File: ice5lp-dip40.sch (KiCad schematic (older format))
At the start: 45 parts, among them J1 Conn_02x04_Odd_Even, J2 Conn_01x20, J3 Conn_01x20, J4 USB_B_Micro, SW1 SW_Push, SW2 SW_Push, U1 AT25D011-SSHF, U2 MIC5355-S4YMME, U3 ICE5LP4K-SG48, X1 ECS-2520MV-500-BN-TR

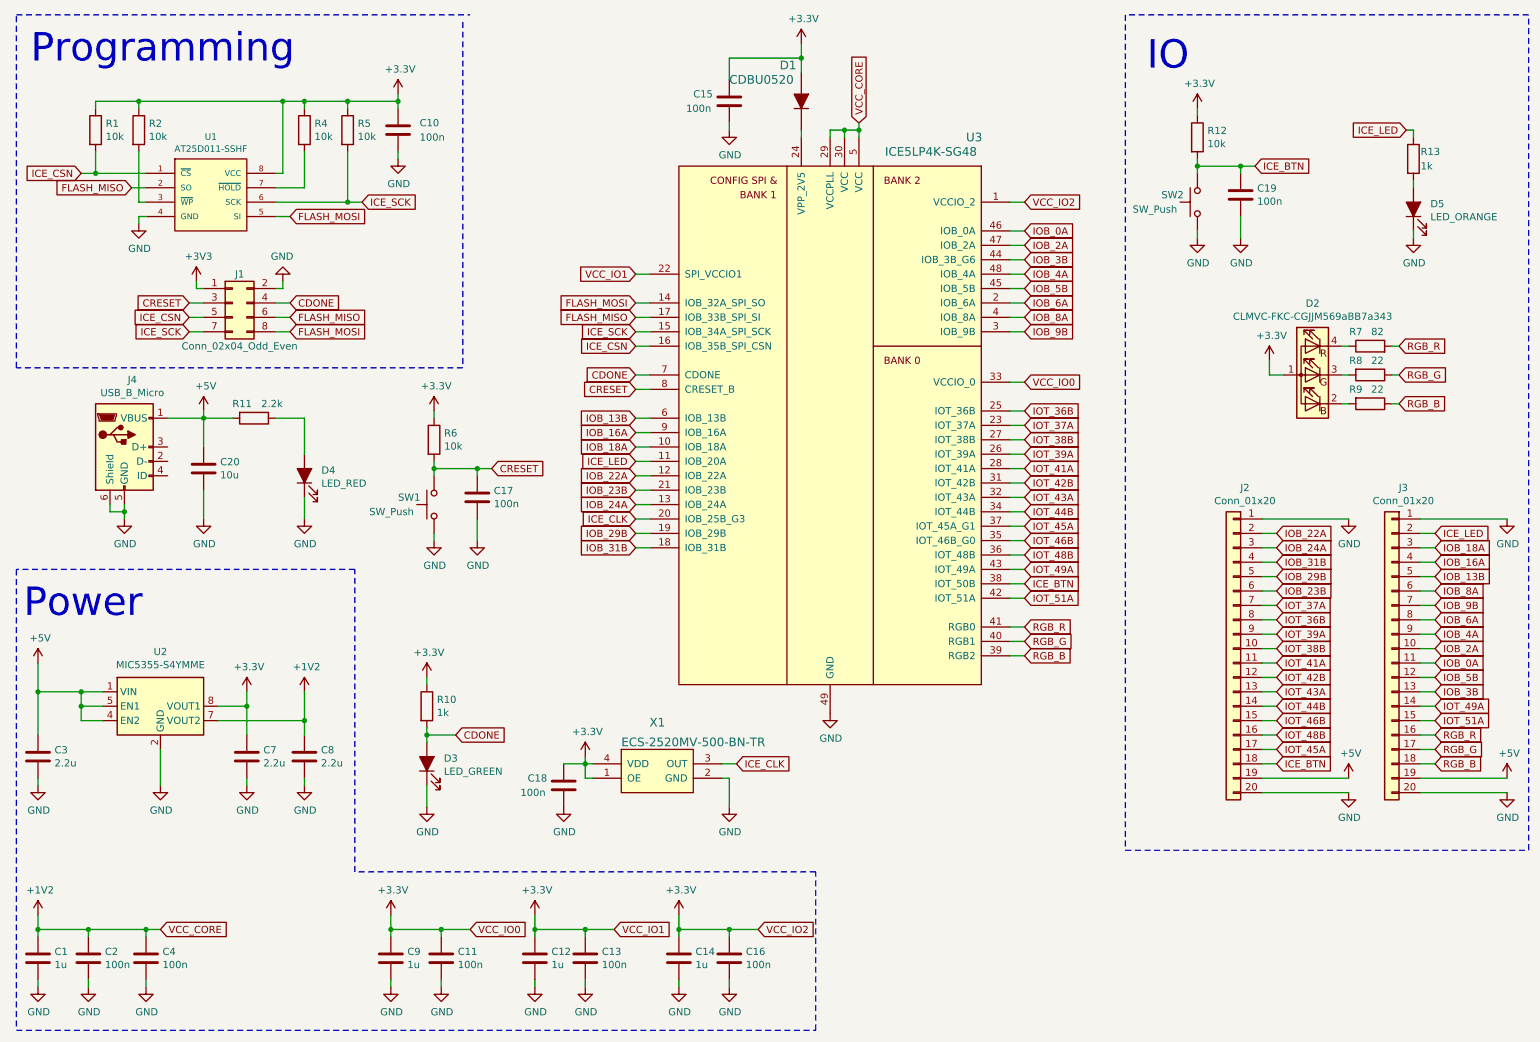
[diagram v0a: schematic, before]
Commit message: Beautify schematic and place all components on PCB
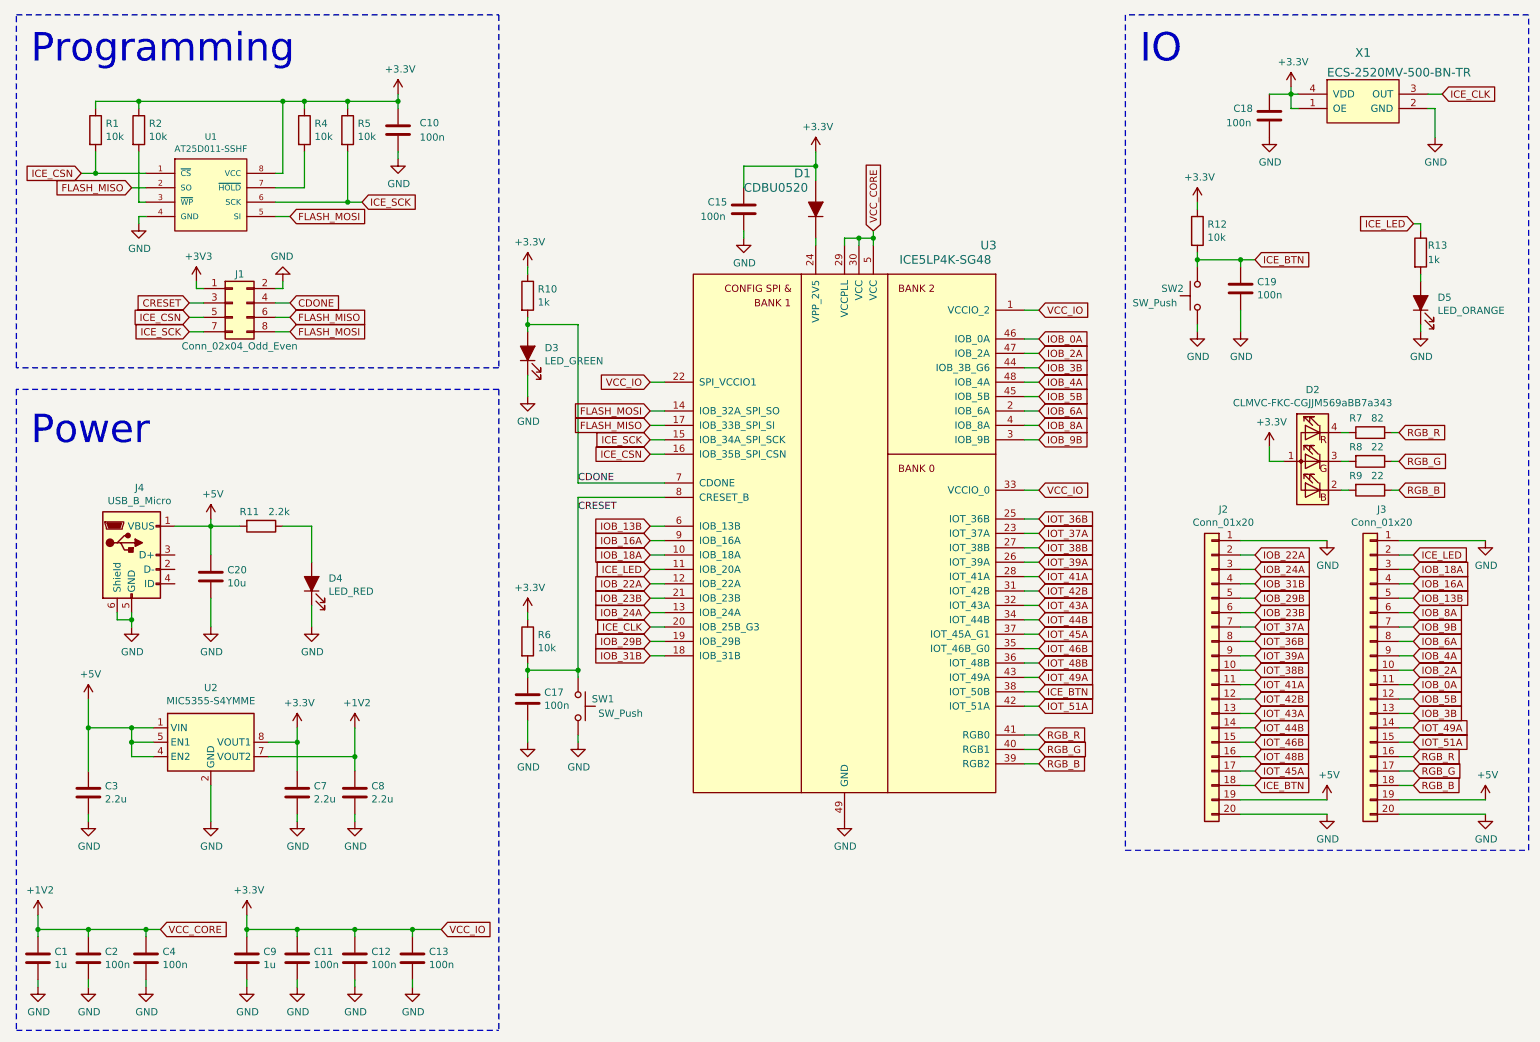
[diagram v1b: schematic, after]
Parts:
- removed C14: 1u, esynr3z_Capacitor:C_0603, symbol Device:C
- removed C16: 100n, esynr3z_Capacitor:C_0603, symbol Device:C
- C12: value 1u -> 100n
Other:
- moved on the sheet: C11, C12, C13, C15, C17, C18, C19, C20, C3, C7, C8, C9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

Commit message: Make footprints local
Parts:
- C1, C10, C11, C12, C13, C15, C17, C18, C19, C2, C20, C3, C4, C7, C8, C9: footprint esynr3z_Capacitor:C_0603 -> lib_fp:C_0603
- D1: footprint esynr3z_Diode:SOD-523F -> lib_fp:SOD-523F
- D2: footprint esynr3z_LED:LED_Cree-PLCC4_2x2mm_CW -> lib_fp:LED_Cree-PLCC4_2x2mm_CW
- D3, D4, D5: footprint esynr3z_LED:LED_0603 -> lib_fp:LED_0603
- J1: footprint esynr3z_Connector:PinHeader_2x04_P2.54mm_Vertical -> lib_fp:PinHeader_2x04_P2.54mm_Vertical
- J2, J3: footprint esynr3z_Connector:PinHeader_1x20_P2.54mm_Vertical -> lib_fp:PinHeader_1x20_P2.54mm_Vertical
- J4: footprint esynr3z_ConnectorUSB:USB_Micro-B_Wurth_629105136821 -> lib_fp:USB_Micro-B_Wurth_629105136821
- R1, R10, R11, R12, R13, R2, R4, R5, R6, R7, R8, R9: footprint esynr3z_Resistor:R_0603 -> lib_fp:R_0603
- SW1, SW2: footprint esynr3z_Switch:PTS830 -> lib_fp:PTS830
- U1: footprint esynr3z_SO:SOIC-8_3.9x4.9mm_P1.27mm -> lib_fp:SOIC-8_3.9x4.9mm_P1.27mm
- U2: footprint esynr3z_SO:MSOP-8-1EP_3x3mm_P0.65mm_EP2.54x2.8mm_ThermalVias -> lib_fp:MSOP-8-1EP_3x3mm_P0.65mm_EP2.54x2.8mm_ThermalVias
- U3: footprint esynr3z_QFN:QFN-48-1EP_7x7mm_P0.5mm_EP5x5mm_ThermalVias -> lib_fp:QFN-48-1EP_7x7mm_P0.5mm_EP5x5mm_ThermalVias
- X1: footprint esynr3z_Oscillator:ECS-2520MV_4Pin_2.5x2.0mm -> lib_fp:ECS-2520MV_4Pin_2.5x2.0mm

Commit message: Make symbols project local
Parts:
- C1, C10, C11, C12, C13, C15, C17, C18, C19, C2, C20, C3, C4, C7, C8, C9: symbol Device:C -> ice5lp-dip40:Device_C
- D1: symbol esynr3z_DiodeRectifier:CDBU0520 -> ice5lp-dip40:esynr3z_DiodeRectifier_CDBU0520
- D2: symbol esynr3z_LED:CLMVC-FKC-CGJJM569aBB7a343 -> ice5lp-dip40:esynr3z_LED_CLMVC-FKC-CGJJM569aBB7a343
- D3, D4, D5: symbol Device:LED_ALT -> ice5lp-dip40:Device_LED_ALT
- J1: symbol Connector_Generic:Conn_02x04_Odd_Even -> ice5lp-dip40:Connector_Generic_Conn_02x04_Odd_Even
- J2, J3: symbol Connector_Generic:Conn_01x20 -> ice5lp-dip40:Connector_Generic_Conn_01x20
- J4: symbol Connector:USB_B_Micro -> ice5lp-dip40:Connector_USB_B_Micro
- R1, R10, R11, R12, R13, R2, R4, R5, R6, R7, R8, R9: symbol Device:R -> ice5lp-dip40:Device_R
- SW1, SW2: symbol Switch:SW_Push -> ice5lp-dip40:Switch_SW_Push
- U1: symbol esynr3z_MemoryFlash:AT25D011-SSHF -> ice5lp-dip40:esynr3z_MemoryFlash_AT25D011-SSHF
- U2: symbol esynr3z_RegulatorLinear:MIC5355-S4YMME -> ice5lp-dip40:esynr3z_RegulatorLinear_MIC5355-S4YMME
- U3: symbol esynr3z_FPGA:ICE5LP4K-SG48 -> ice5lp-dip40:esynr3z_FPGA_ICE5LP4K-SG48
- X1: symbol esynr3z_Oscillator:ECS-2520MV-500-BN-TR -> ice5lp-dip40:esynr3z_Oscillator_ECS-2520MV-500-BN-TR

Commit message: Replace 1Mb flash with 8Mb one
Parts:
- removed U1: AT25D011-SSHF, lib_fp:SOIC-8_3.9x4.9mm_P1.27mm, symbol ice5lp-dip40:esynr3z_MemoryFlash_AT25D011-SSHF
- added U1: AT25D081-SSHD, lib_fp:SOIC-8_3.9x4.9mm_P1.27mm, symbol ice5lp-dip40:esynr3z_MemoryFlash_AT25D081-SSHD
- U3: Lanufacturer Lattice -> (none)
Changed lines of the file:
@@
 EESchema Schematic File Version 4
-LIBS:ice5lp-dip40-cache
 EELAYER 26 0
 EELAYER END
@@
 F 2 "lib_fp:QFN-48-1EP_7x7mm_P0.5mm_EP5x5mm_ThermalVias" H 7850 6450 50  0001 C CNN
 F 3 "" H 5700 5200 50  0001 C CNN
-F 4 "Lattice" H 6950 6350 50  0001 C CNN "Lanufacturer"
 	1    6350 4200
 	1    0    0    -1
@@
 	2950 5750 2950 5850
 Connection ~ 2950 5750
-$Comp
-L ice5lp-dip40:esynr3z_MemoryFlash_AT25D011-SSHF U1
-U 1 1 5B52E310
-P 1950 1850
-F 0 "U1" H 1950 2254 45  0000 C CNN
-F 1 "AT25D011-SSHF" H 1950 2170 45  0000 C CNN
-F 2 "lib_fp:SOIC-8_3.9x4.9mm_P1.27mm" H 2300 2200 20  0001 C CNN
-F 3 "" H 1550 2150 50  0001 C CNN
-	1    1950 1850
-	1    0    0    -1
-$EndComp
 $Comp
 L ice5lp-dip40:power_GND #PWR0133
@@
 Text Label 4500 4050 0    50   ~ 0
 CRESET
+$Comp
+L ice5lp-dip40:esynr3z_MemoryFlash_AT25D081-SSHD U1
+U 1 1 5BA61AF9
+P 1950 1850
+F 0 "U1" H 1950 2254 45  0000 C CNN
+F 1 "AT25D081-SSHD" H 1950 2170 45  0000 C CNN
+F 2 "lib_fp:SOIC-8_3.9x4.9mm_P1.27mm" H 2300 2200 20  0001 C CNN
+F 3 "https://www.adestotech.com/wp-content/uploads/DS-AT25SF081_045.pdf" H 2500 2300 50  0001 C CNN
+	1    1950 1850
+	1    0    0    -1
+$EndComp
 $EndSCHEMATC

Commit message: Trace USB data lines into fpga
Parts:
- added R14, R15: 68, lib_fp:R_0603, symbol ice5lp-dip40:Device_R
- added R3: 1.5k, lib_fp:R_0603, symbol ice5lp-dip40:Device_R
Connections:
- net labels added: USB_N, USB_P, USB_PU
- net labels removed: IOT_44B, IOT_46B, IOT_48B
- wire segments 229 -> 239
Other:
- moved on the sheet: C20, D4, R11
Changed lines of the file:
@@
 EESchema Schematic File Version 4
+LIBS:ice5lp-dip40-cache
 EELAYER 26 0
 EELAYER END
@@
 Text GLabel 7700 4700 2    50   Input ~ 0
 IOT_43A
-Text GLabel 7700 4800 2    50   Input ~ 0
-IOT_44B
 Text GLabel 7700 4900 2    50   Input ~ 0
 IOT_45A
-Text GLabel 7700 5000 2    50   Input ~ 0
-IOT_46B
-Text GLabel 7700 5100 2    50   Input ~ 0
-IOT_48B
 Text GLabel 7700 5200 2    50   Input ~ 0
 IOT_49A
@@
 $EndComp
 Wire Wire Line
-	9100 6150 9700 6150
+	9100 6150 9250 6150
 Wire Wire Line
 	9700 6050 9100 6050
@@
 Wire Wire Line
 	9200 5450 9100 5450
+Wire Wire Line
+	9200 5550 9100 5550
+Wire Wire Line
+	9200 5650 9100 5650
+Wire Wire Line
+	9200 5750 9100 5750
 Text GLabel 9200 5550 2    50   Input ~ 0
-IOT_44B
-Wire Wire Line
-	9200 5550 9100 5550
+IOT_45A
+Wire Wire Line
+	9200 5850 9100 5850
 Text GLabel 9200 5650 2    50   Input ~ 0
-IOT_46B
-Wire Wire Line
-	9200 5650 9100 5650
-Text GLabel 9200 5750 2    50   Input ~ 0
-IOT_48B
-Wire Wire Line
-	9200 5750 9100 5750
-Text GLabel 9200 5850 2    50   Input ~ 0
-IOT_45A
-Wire Wire Line
-	9200 5850 9100 5850
-Text GLabel 9200 5950 2    50   Input ~ 0
 ICE_BTN
-Wire Wire Line
-	9200 5950 9100 5950
 $Comp
 L ice5lp-dip40:esynr3z_LED_CLMVC-FKC-CGJJM569aBB7a343 D2
@@
 L ice5lp-dip40:Device_LED_ALT D4
 U 1 1 5BA2D2CB
-P 2650 4550
-F 0 "D4" V 2688 4432 50  0000 R CNN
-F 1 "LED_RED" V 2597 4432 50  0000 R CNN
-F 2 "lib_fp:LED_0603" H 2650 4550 50  0001 C CNN
-F 3 "~" H 2650 4550 50  0001 C CNN
-	1    2650 4550
+P 3250 4550
+F 0 "D4" V 3288 4432 50  0000 R CNN
+F 1 "LED_RED" V 3197 4432 50  0000 R CNN
+F 2 "lib_fp:LED_0603" H 3250 4550 50  0001 C CNN
+F 3 "~" H 3250 4550 50  0001 C CNN
+	1    3250 4550
 	0    -1   -1   0
 $EndComp
@@
 L ice5lp-dip40:power_GND #PWR0150
 U 1 1 5BA2D2D2
-P 2650 4850
-F 0 "#PWR0150" H 2650 4600 50  0001 C CNN
-F 1 "GND" H 2655 4677 50  0000 C CNN
-F 2 "" H 2650 4850 50  0001 C CNN
-F 3 "" H 2650 4850 50  0001 C CNN
-	1    2650 4850
+P 3250 4850
+F 0 "#PWR0150" H 3250 4600 50  0001 C CNN
+F 1 "GND" H 3255 4677 50  0000 C CNN
+F 2 "" H 3250 4850 50  0001 C CNN
+F 3 "" H 3250 4850 50  0001 C CNN
+	1    3250 4850
 	1    0    0    -1
 $EndComp
@@
 L ice5lp-dip40:Device_R R11
 U 1 1 5BA2D2D8
-P 2300 4150
-F 0 "R11" V 2200 4000 50  0000 L CNN
-F 1 "2.2k" V 2200 4200 50  0000 L CNN
-F 2 "lib_fp:R_0603" V 2230 4150 50  0001 C CNN
-F 3 "~" H 2300 4150 50  0001 C CNN
-	1    2300 4150
+P 3050 4150
+F 0 "R11" V 2950 4050 50  0000 L CNN
+F 1 "2.2k" V 3050 4050 50  0000 L CNN
+F 2 "lib_fp:R_0603" V 2980 4150 50  0001 C CNN
+F 3 "~" H 3050 4150 50  0001 C CNN
+	1    3050 4150
 	0    1    1    0
 $EndComp
 Wire Wire Line
-	2650 4850 2650 4700
+	3250 4850 3250 4700
 $Comp
 L ice5lp-dip40:Device_LED_ALT D5
@@
 L ice5lp-dip40:power_+5V #PWR0153
 U 1 1 5BB7791B
-P 1950 4100
-F 0 "#PWR0153" H 1950 3950 50  0001 C CNN
-F 1 "+5V" H 1965 4273 50  0000 C CNN
-F 2 "" H 1950 4100 50  0001 C CNN
-F 3 "" H 1950 4100 50  0001 C CNN
-	1    1950 4100
-	1    0    0    -1
-$EndComp
-Wire Wire Line
-	1700 4150 1950 4150
-Wire Wire Line
-	1950 4150 1950 4100
+P 2800 4100
+F 0 "#PWR0153" H 2800 3950 50  0001 C CNN
+F 1 "+5V" H 2815 4273 50  0000 C CNN
+F 2 "" H 2800 4100 50  0001 C CNN
+F 3 "" H 2800 4100 50  0001 C CNN
+	1    2800 4100
+	1    0    0    -1
+$EndComp
+Wire Wire Line
+	2800 4150 2800 4100
 $Comp
 L ice5lp-dip40:Device_C C20
 U 1 1 5BB9F4F5
-P 1950 4500
-F 0 "C20" H 2065 4546 50  0000 L CNN
-F 1 "10u" H 2065 4455 50  0000 L CNN
-F 2 "lib_fp:C_0603" H 1988 4350 50  0001 C CNN
-F 3 "~" H 1950 4500 50  0001 C CNN
-	1    1950 4500
+P 2800 4500
+F 0 "C20" H 2915 4546 50  0000 L CNN
+F 1 "10u" H 2915 4455 50  0000 L CNN
+F 2 "lib_fp:C_0603" H 2838 4350 50  0001 C CNN
+F 3 "~" H 2800 4500 50  0001 C CNN
+	1    2800 4500
 	1    0    0    -1
 $EndComp
@@
 L ice5lp-dip40:power_GND #PWR0154
 U 1 1 5BB9F4FC
-P 1950 4850
-F 0 "#PWR0154" H 1950 4600 50  0001 C CNN
-F 1 "GND" H 1955 4677 50  0000 C CNN
-F 2 "" H 1950 4850 50  0001 C CNN
-F 3 "" H 1950 4850 50  0001 C CNN
-	1    1950 4850
-	1    0    0    -1
-$EndComp
-Wire Wire Line
-	1950 4850 1950 4650
-Wire Wire Line
-	1950 4350 1950 4150
-Connection ~ 1950 4150
-Wire Wire Line
-	1950 4150 2150 4150
-Wire Wire Line
-	2650 4150 2450 4150
-Wire Wire Line
-	2650 4150 2650 4400
+P 2800 4850
+F 0 "#PWR0154" H 2800 4600 50  0001 C CNN
+F 1 "GND" H 2805 4677 50  0000 C CNN
+F 2 "" H 2800 4850 50  0001 C CNN
+F 3 "" H 2800 4850 50  0001 C CNN
+	1    2800 4850
+	1    0    0    -1
+$EndComp
+Wire Wire Line
+	2800 4850 2800 4650
+Wire Wire Line
+	2800 4350 2800 4150
+Connection ~ 2800 4150
+Wire Wire Line
+	2800 4150 2900 4150
+Wire Wire Line
+	3250 4150 3200 4150
+Wire Wire Line
+	3250 4150 3250 4400
 $Comp
 L ice5lp-dip40:Connector_USB_B_Micro J4
@@
 	1    0    0    -1
 $EndComp
+$Comp
+L ice5lp-dip40:Device_R R15
+U 1 1 5BA8B82A
+P 2000 4450
+F 0 "R15" V 1900 4350 50  0000 L CNN
+F 1 "68" V 2000 4400 50  0000 L CNN
+F 2 "lib_fp:R_0603" V 1930 4450 50  0001 C CNN
+F 3 "~" H 2000 4450 50  0001 C CNN
+	1    2000 4450
+	0    -1   -1   0
+$EndComp
+$Comp
+L ice5lp-dip40:Device_R R14
+U 1 1 5BAA6B37
+P 2000 4350
+F 0 "R14" V 2100 4250 50  0000 L CNN
+F 1 "68" V 2000 4300 50  0000 L CNN
+F 2 "lib_fp:R_0603" V 1930 4350 50  0001 C CNN
+F 3 "~" H 2000 4350 50  0001 C CNN
+	1    2000 4350
+	0    -1   -1   0
+$EndComp
+$Comp
+L ice5lp-dip40:Device_R R3
+U 1 1 5BAB46BF
+P 1800 4650
+F 0 "R3" H 1850 4650 50  0000 L CNN
+F 1 "1.5k" H 1850 4550 50  0000 L CNN
+F 2 "lib_fp:R_0603" V 1730 4650 50  0001 C CNN
+F 3 "~" H 1800 4650 50  0001 C CNN
+	1    1800 4650
+	1    0    0    -1
+$EndComp
+Text GLabel 2200 4350 2    50   Input ~ 0
+USB_P
+Wire Wire Line
+	2200 4350 2150 4350
+Text GLabel 2200 4450 2    50   Input ~ 0
+USB_N
+Wire Wire Line
+	2200 4450 2150 4450
+Wire Wire Line
+	1700 4350 1800 4350
+Wire Wire Line
+	1700 4450 1850 4450
+Wire Wire Line
+	1800 4500 1800 4350
+Connection ~ 1800 4350
+Wire Wire Line
+	1800 4350 1850 4350
+Wire Wire Line
+	1800 4800 1800 4850
+Wire Wire Line
+	1800 4850 2200 4850
+Text GLabel 2200 4850 2    50   Input ~ 0
+USB_PU
+Wire Wire Line
+	1700 4150 2800 4150
+Text GLabel 7700 5000 2    50   Input ~ 0
+USB_P
+Text GLabel 7700 4800 2    50   Input ~ 0
+USB_N
+Text GLabel 7700 5100 2    50   Input ~ 0
+USB_PU
+Wire Wire Line
+	9250 5950 9250 6150
+Wire Wire Line
+	9100 5950 9250 5950
+Connection ~ 9250 6150
+Wire Wire Line
+	9250 6150 9700 6150
+Text GLabel 9200 5850 2    50   Input ~ 0
+VCC_IO
+Text GLabel 9200 5750 2    50   Input ~ 0
+VCC_CORE
 $EndSCHEMATC

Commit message: Update docs and generator info
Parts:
- X1: value ECS-2520MV-500-BN-TR -> ECS-2520MV-120-BN-TR; symbol ice5lp-dip40:esynr3z_Oscillator_ECS-2520MV-500-BN-TR -> ice5lp-dip40:esynr3z_Oscillator_ECS-2520MV-XXX
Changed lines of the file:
@@
 Title "Lattice iCE5LP4K DIP40 breakout board"
 Date "2018-07-23"
-Rev "v1.0"
+Rev "A"
 Comp ""
 Comment1 ""
@@
 $EndComp
 $Comp
-L ice5lp-dip40:esynr3z_Oscillator_ECS-2520MV-500-BN-TR X1
+L ice5lp-dip40:esynr3z_Oscillator_ECS-2520MV-XXX X1
 U 1 1 5B84C298
 P 9950 1200
 F 0 "X1" H 9950 1537 60  0000 C CNN
-F 1 "ECS-2520MV-500-BN-TR" H 10200 1400 60  0000 C CNN
+F 1 "ECS-2520MV-120-BN-TR" H 10200 1400 60  0000 C CNN
 F 2 "lib_fp:ECS-2520MV_4Pin_2.5x2.0mm" H 10350 1700 60  0001 L CNN
 F 3 "lib_fp://www.ecsxtal.com/store/pdf/ECS-2520MV.pdf" H 10350 1800 60  0001 L CNN
